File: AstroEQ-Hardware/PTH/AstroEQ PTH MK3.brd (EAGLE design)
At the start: 100 x 66 mm, 43 parts, among them IC1 ATMEGA162-16PU, IC2 PIC18F14K50-I/P, IC3 78L05, J1 POWER_JACKPTH, M1 Motor Driver, M2 Motor Driver, X1 16MHz, X2 12MHz

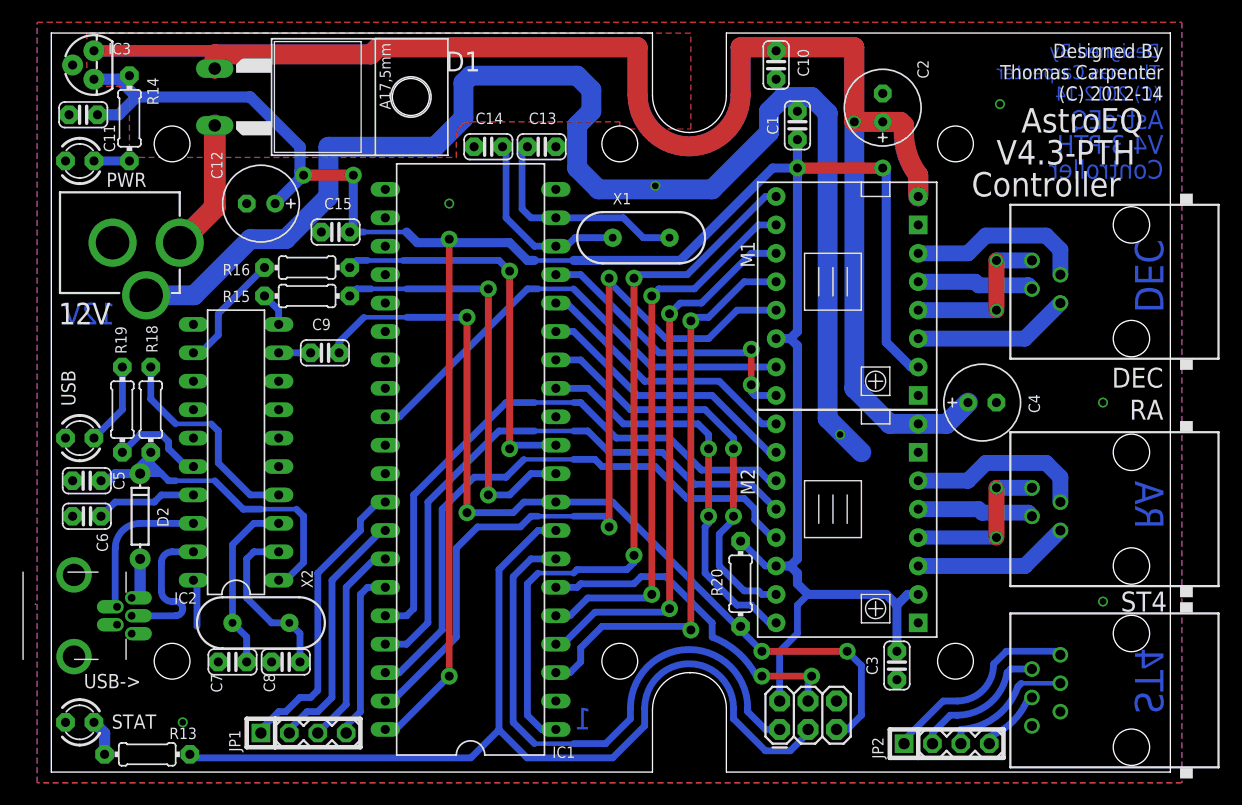
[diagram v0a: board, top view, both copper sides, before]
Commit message: Update DIY Eagle Designs
(1) Bring AstroEQ-DIY up to date (V4.4)
(2) Export AstroEQ-DIY schematic to PDF
(3) Make sure the etch file doesn't have holes in pads
(4) Add AstroEQ-ARD variant - Arduino Mega sheild
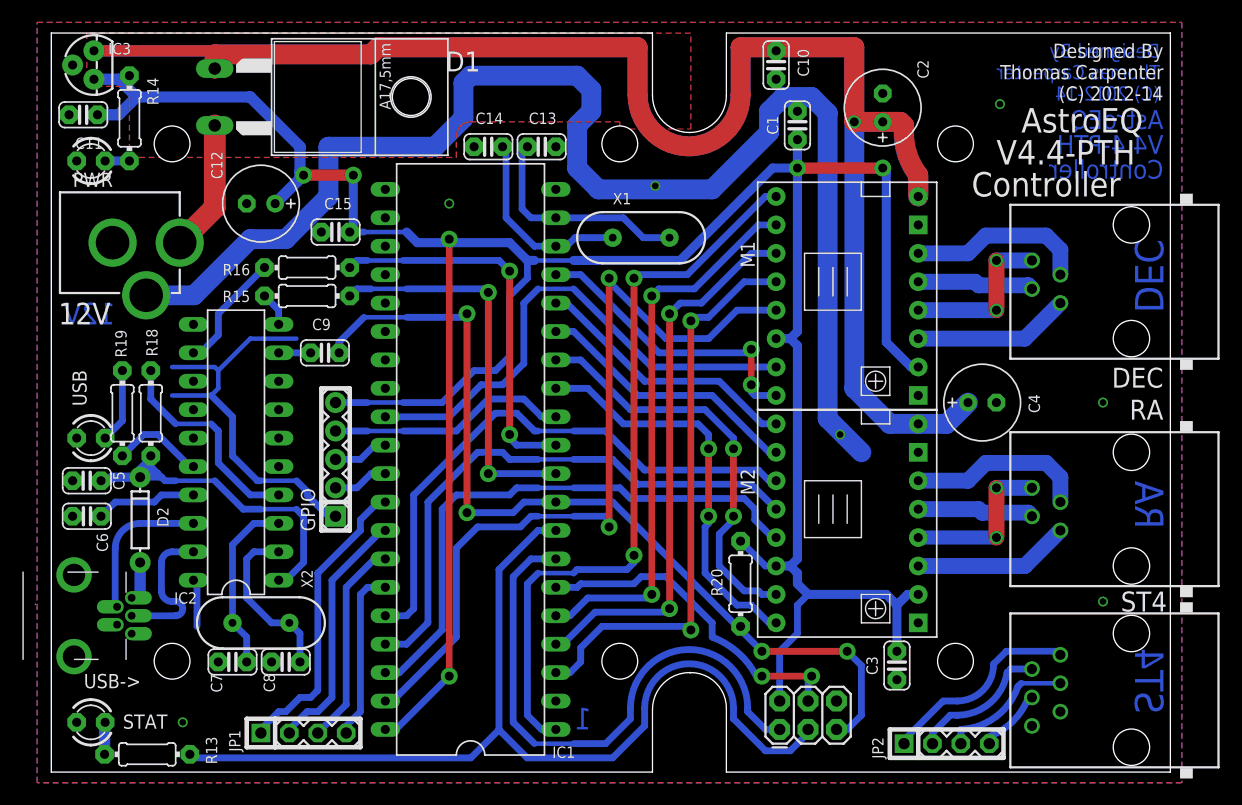
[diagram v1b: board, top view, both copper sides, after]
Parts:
- added GPIO: (no value), SparkFun:1X05
- moved PWR 1.00 mm to (3.54, 54.6)
- moved STAT 1.00 mm to (3.54, 4.45)
- moved USB 1.00 mm to (3.54, 29.8)
- moved D2 0.32 mm to (7.94, 22.5)
- moved R18 0.32 mm to (8.89, 32.1)
- moved R19 0.32 mm to (6.35, 32.1)
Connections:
- new net IO0: GPIO.4, IC1.12
- new net IO1: GPIO.3, IC1.30
- new net IO2: GPIO.2, IC1.31
- net +5V: now also GPIO.5
- net GND: now also GPIO.1
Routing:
- net GND: track 124.5 -> 160.8 mm
- net +5V: track 234.8 -> 261.3 mm
- net IO0: track 0.00 -> 21.5 mm
- net IO2: track 0.00 -> 4.97 mm
- net IO1: track 0.00 -> 4.97 mm
- net STEP-1: track 42.6 -> 45.7 mm
- net TX: track 37.9 -> 35.0 mm
- net !RST-2: track 52.6 -> 50.5 mm
- net MS3-2: track 52.0 -> 50.5 mm
- net PWRLED: track 3.18 -> 2.18 mm
- net RX: track 35.1 -> 34.3 mm
- net MS2-2: track 51.7 -> 50.9 mm
- net USBLED: track 7.40 -> 6.67 mm
- net VPIC: track 32.9 -> 32.3 mm
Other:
- board text added: "V4.4-PTH"
- board text removed: "V4.3-PTH"

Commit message: Update PCB Logo
Add AstroEQ logo to PCB hardware designs.
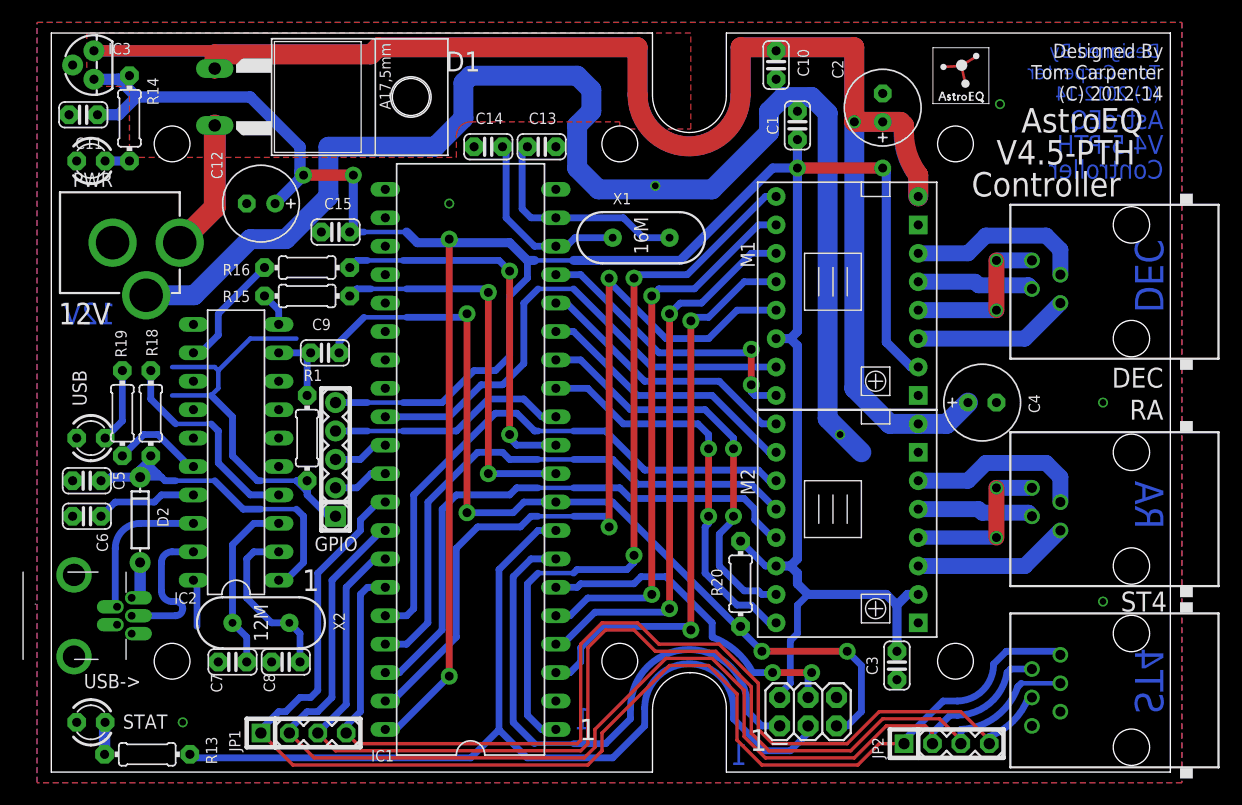
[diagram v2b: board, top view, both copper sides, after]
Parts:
- added LOGO1: ASTROEQ5MM, CompanyLogos:ASTROEQ-SMALL
- added R1: 10k, rcl:0204/7
- moved PROG 0.32 mm to (65.1, 4.13)
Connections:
- removed net DEC+B: JP2.2, ST4.5
- removed net DEC-B: JP2.3, ST4.4
- removed net RA+B: JP2.1, ST4.6
- removed net RA-B: JP2.4, ST4.3
- net DEC+: now also JP2.2, ST4.5
- net DEC-: now also JP2.3, ST4.4
- net DTR: now also R1.1
- net GND: now also R1.2
- net RA+: now also JP2.1, ST4.6
- net RA-: now also JP2.4, ST4.3
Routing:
- net DEC-: track 18.6 -> 107.0 mm
- net RA+: track 26.5 -> 114.4 mm
- net DEC+: track 22.4 -> 105.9 mm
- net RA-: track 15.4 -> 98.1 mm
- net RA+B: track 17.7 -> 0.00 mm
- net DEC+B: track 12.0 -> 0.00 mm
- net DEC-B: track 11.6 -> 0.00 mm
- net RA-B: track 5.89 -> 0.00 mm
- net DTR: track 2.86 -> 6.98 mm
- net GND: track 160.8 -> 162.7 mm
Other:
- board text added: "12M"
- board text added: "16M"
- board text added: "Tom Carpenter"
- board text added: "V4.5-PTH"
- board text removed: "Thomas Carpenter"
- board text removed: "V4.4-PTH"

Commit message: Update Hardware Files
Update the repository to contain the latest hardware designs for AstroEQ
V4.6, along with exported BOM.
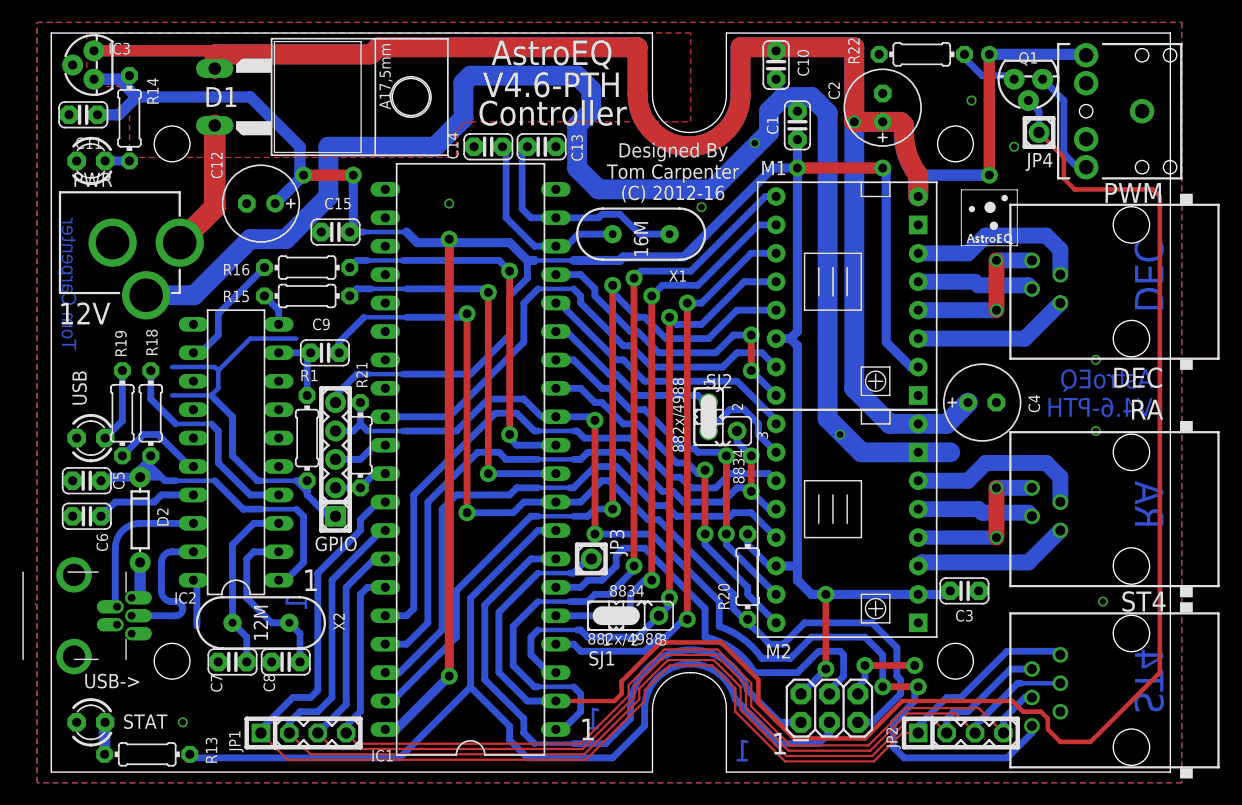
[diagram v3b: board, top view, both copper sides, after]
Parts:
- added J2, J3: (no value), jumper:JUMP
- added JP3, JP4: M01PTH, SparkFun:1X01
- added PWM: JACK, SparkFun:AUDIO-JACK
- added Q1: BS270, SparkFun:TO-92
- added R21: 1k, rcl:0204/7
- added R22: 120, rcl:0204/7
- added SJ1: (no value), jumper:JP2
- added SJ2: (no value), jumper:JP2L
- HAMMOND-1593N: value HAMMOND-1593N -> HAMMOND-1593N-4HOLE; device holes:HAMMOND-1593N -> holes:HAMMOND-1593N4HOLES
- moved LOGO1 13.0 mm to (81.3, 47.0)
- moved C3 8.99 mm to (81.6, 16.2), turned to 0 degrees
- moved PROG 1.93 mm to (67.0, 4.45)
- moved JP2 1.59 mm to (77.5, 3.49)
- moved R20 0.90 mm to (62.2, 17.5)
- moved X1 0.32 mm to (52.7, 48.1)
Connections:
- net DEC+ renamed DEC+/SI
- net DEC- renamed DEC-/CK
- net RA+ renamed RA+/SO
- net RA- renamed RA-/!SS
- new net MS13-1: M1.2, SJ1.2
- new net MS13-2: M2.2, SJ2.2
- new net N$2: PWM.RING, Q1.1
- new net N$4: Q1.3, R22.2
- new net PWM: IC1.2, JP3.1, JP4.1, Q1.2
- net GND: now also PWM.SLEEVE, R22.1
- net IO0: now also R21.1, ST4.1
- net IO2: now also R21.2
- net MS1-1: now also SJ1.1; no longer M1.2
- net MS1-2: now also SJ2.1; no longer M2.2
- net MS3-1: now also SJ1.3
- net MS3-2: now also SJ2.3
- net V+: now also PWM.TIP
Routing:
- net PWM: track 0.00 -> 149.4 mm
- net IO0: track 21.5 -> 97.4 mm, vias 0 -> 4
- net MS1-1: track 49.8 -> 4.13 mm, vias 2 -> 0
- net MS13-1: track 0.00 -> 43.5 mm, vias 0 -> 2
- net V+: track 230.5 -> 256.3 mm, vias 1 -> 3
- net GND: track 162.7 -> 177.9 mm, vias 7 -> 12
- net N$2: track 0.00 -> 9.93 mm
- net MS13-2: track 0.00 -> 9.28 mm
- net RESET: track 80.0 -> 88.8 mm, vias 4 -> 2
- net MOSI: track 29.8 -> 38.5 mm, vias 2 -> 0
- net DEC-/CK: track 107.0 -> 98.7 mm
- net MS1-2: track 24.2 -> 16.3 mm
- net RA-/!SS: track 98.1 -> 90.2 mm
- net MS3-2: track 50.5 -> 58.0 mm, vias 0 -> 2
- net N$4: track 0.00 -> 5.55 mm
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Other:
- board text added: "(C) 2012-16"
- board text added: "882x/4988"
- board text added: "8834"
- board text added: "V4.6-PTH"
- board text removed: "(C) 2012-14"
- board text removed: "Sq Pad"
- board text removed: "V4.5-PTH"
